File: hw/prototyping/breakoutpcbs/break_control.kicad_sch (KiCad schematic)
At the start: 21 parts, among them J11 Conn_01x07, J12 Conn_01x07, J13 Conn_01x06, J15 Conn_01x04, J16 Screw_Terminal_01x04, J17 Conn_01x05, J18 Screw_Terminal_01x04, Q10 BC337, Q11 BC847

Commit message: fixed wrong pinout on rf module and updated footprints
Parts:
- removed M2: ~, chinese_modules:RF_controller, symbol chinese_modules:RF_controller
- added M3: ~, chinese_modules:RF_controller, symbol chinese_modules:RF_controller
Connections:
- net +5V_1: now also M3.6 (V+)
- net GND4: now also M3.7 (GND)
- net at R40.2: now also M3.5 (D0)
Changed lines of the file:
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@@
-	)
-	(symbol
-		(lib_id "chinese_modules:RF_controller")
-		(at 67.31 48.26 0)
-		(unit 1)
-		(exclude_from_sim no)
-		(in_bom yes)
-		(on_board yes)
-		(dnp no)
-		(fields_autoplaced yes)
-		(property "Reference" "M2"
-			(at 67.31 34.29 0)
-			(effects
-				(font
-					(size 1.27 1.27)
-				)
-			)
-		)
-		(property "Value" "~"
-			(at 67.31 36.83 0)
-			(effects
-				(font
-					(size 1.27 1.27)
-				)
-			)
-		)
-		(property "Footprint" "chinese_modules:RF_controller"
-			(at 67.31 48.26 0)
-			(effects
-				(font
-					(size 1.27 1.27)
-				)
-				(hide yes)
-			)
-		)
-		(property "Datasheet" ""
-			(at 67.31 48.26 0)
-			(effects
-				(font
-					(size 1.27 1.27)
-				)
-				(hide yes)
-			)
-		)
-		(property "Description" ""
-			(at 67.31 48.26 0)
-			(effects
-				(font
-					(size 1.27 1.27)
-				)
-				(hide yes)
-			)
-		)
-		(pin "8"
-		)
-		(pin "2"
-		)
-		(pin "1"
-		)
-		(pin "5"
-		)
-		(pin "6"
-		)
-		(pin "7"
-		)
-		(pin "3"
-		)
-		(pin "4"
-		)
-		(instances
-			(project "breakoutpcbs"
-				(path "/164def8b-47e5-45df-ad5a-f5307e8b0f23/6473b973-a331-47c6-86ec-edf4d9af8870"
-					(reference "M2")
-					(unit 1)
-				)
-			)
-		)
 	)
 	(symbol
@@
 					(unit 1)
 				)
+			)
+		)
+	)
+	(symbol
+		(lib_name "RF_controller_1")
+		(lib_id "chinese_modules:RF_controller")
+		(at 67.31 48.26 0)
+		(unit 1)
+		(exclude_from_sim no)
+		(in_bom yes)
+		(on_board yes)
+		(dnp no)
+		(fields_autoplaced yes)
+		(property "Reference" "M3"
+			(at 67.31 34.29 0)
+			(effects
+				(font
+					(size 1.27 1.27)
+				)
+			)
+		)
+		(property "Value" "~"
+			(at 67.31 36.83 0)
+			(effects
+				(font
+					(size 1.27 1.27)
+				)
+			)
+		)
+		(property "Footprint" "chinese_modules:RF_controller"
+			(at 67.31 48.26 0)
+			(effects
+				(font
+					(size 1.27 1.27)
+				)
+				(hide yes)
+			)
+		)
+		(property "Datasheet" ""
+			(at 67.31 48.26 0)
+			(effects
+				(font
+					(size 1.27 1.27)
+				)
+				(hide yes)
+			)
+		)
+		(property "Description" ""
+			(at 67.31 48.26 0)
+			(effects
+				(font
+					(size 1.27 1.27)
+				)
+				(hide yes)
+			)
+		)
+		(pin "7"
+		)
+		(pin "4"
+		)
+		(pin "3"
+		)
+		(pin "5"
+		)
+		(pin "6"
+		)
+		(pin "2"
+		)
+		(pin "1"
+		)
+		(pin "8"
+		)
+		(instances
+			(project ""
+				(path "/164def8b-47e5-45df-ad5a-f5307e8b0f23/6473b973-a331-47c6-86ec-edf4d9af8870"
+					(reference "M3")
+					(unit 1)
+				)

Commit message: updated schematics
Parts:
- R40: value 4k7 -> 2k7
- R41: value 10k -> 4k7
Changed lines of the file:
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@@
 			)
 		)
-		(property "Value" "10k"
+		(property "Value" "4k7"
 			(at 98.552 48.26 0)
 			(effects
@@
 			)
 		)
-		(property "Value" "4k7"
+		(property "Value" "2k7"
 			(at 87.63 46.736 90)
 			(effects

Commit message: todos update
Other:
- note added: "TODO: - anode RGB led resistor 1k2 - remove resistors at the cathodes on the RGB LED - 5V DC/DC convertor (stepdown) - connect ledbar to the 5v and make it use the 3v3 while the charging"
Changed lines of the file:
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@@
+		)
+	)
+	(text "TODO: \n- anode RGB led resistor 1k2\n- remove resistors at the cathodes on the RGB LED\n- 5V DC/DC convertor (stepdown)\n- connect ledbar to the 5v and make it use the 3v3 while the charging"
+		(exclude_from_sim no)
+		(at 237.49 56.134 0)
+		(effects
+			(font
+				(size 1.27 1.27)
+			)
 		)
 	)

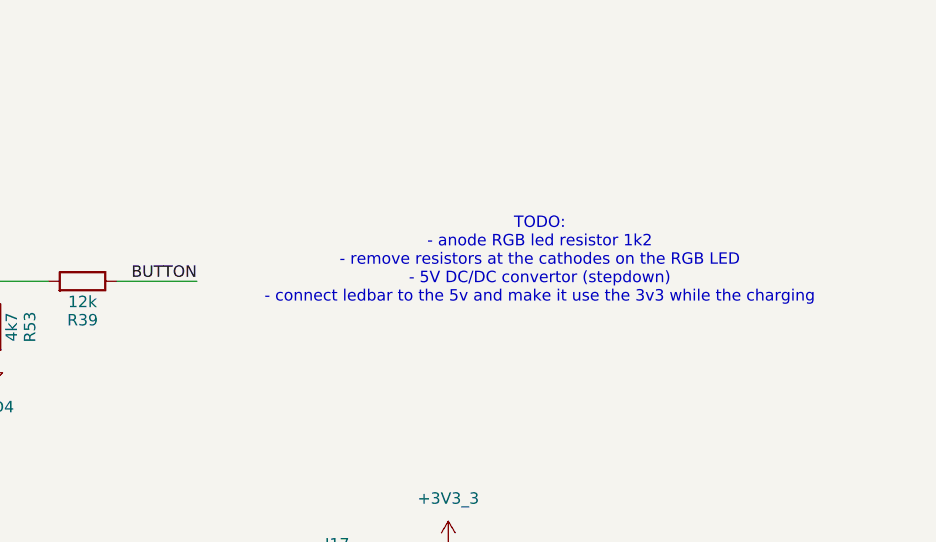
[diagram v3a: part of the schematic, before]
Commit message: added new todos
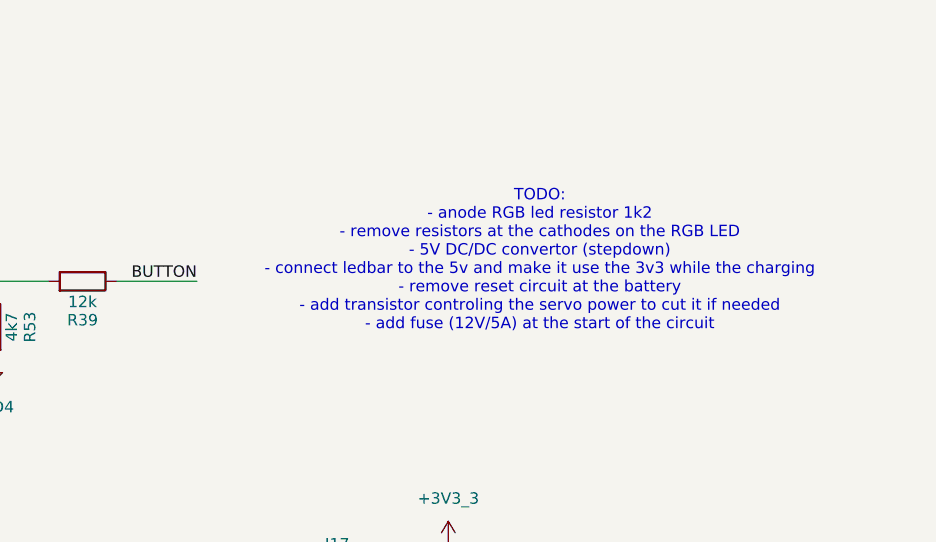
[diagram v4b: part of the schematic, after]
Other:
- note added: "TODO: - anode RGB led resistor 1k2 - remove resistors at the cathodes on the RGB LED - 5V DC/DC convertor (stepdown) - connect ledbar to the 5v and make it use the 3v3 while the charging - remove reset circuit at the battery - add transistor controling the servo power to cut it if needed - add fuse (12V/5A) at the start of the circuit"
- note removed: "TODO: - anode RGB led resistor 1k2 - remove resistors at the cathodes on the RGB LED - 5V DC/DC convertor (stepdown) - connect ledbar to the 5v and make it use the 3v3 while the charging"
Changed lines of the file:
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@@
 		)
 	)
-	(text "TODO: \n- anode RGB led resistor 1k2\n- remove resistors at the cathodes on the RGB LED\n- 5V DC/DC convertor (stepdown)\n- connect ledbar to the 5v and make it use the 3v3 while the charging"
+	(text "TODO: \n- anode RGB led resistor 1k2\n- remove resistors at the cathodes on the RGB LED\n- 5V DC/DC convertor (stepdown)\n- connect ledbar to the 5v and make it use the 3v3 while the charging\n- remove reset circuit at the battery\n- add transistor controling the servo power to cut it if needed\n- add fuse (12V/5A) at the start of the circuit"
 		(exclude_from_sim no)
 		(at 237.49 56.134 0)

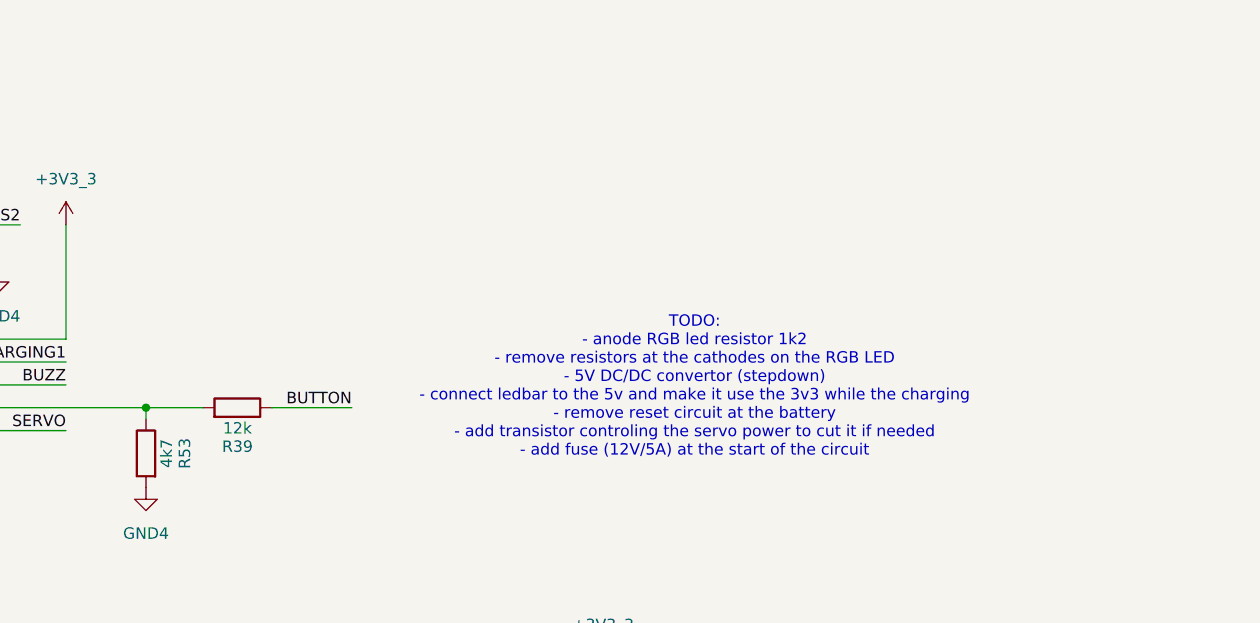
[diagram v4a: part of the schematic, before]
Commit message: updated kicad version and updated todo list with different found issues
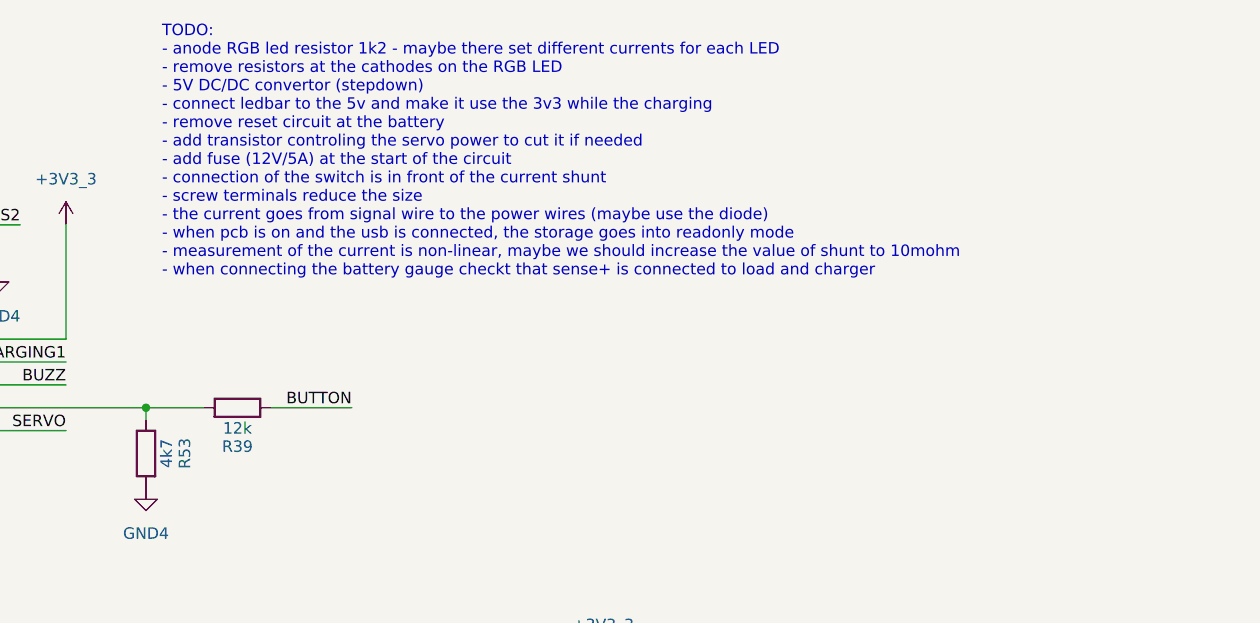
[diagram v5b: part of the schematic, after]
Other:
- note added: "TODO: - anode RGB led resistor 1k2 - maybe there set different currents for each LED - remove resistors at the cathodes on the RGB LED - 5V DC/DC convertor (stepdown) - connect ledbar to the 5v and make it use the 3v3 while the charging - remove reset circuit at the battery - add transistor controling the servo power to cut it if needed - add fuse (12V/5A) at the start of the circuit - connection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"
- note removed: "TODO: - anode RGB led resistor 1k2 - remove resistors at the cathodes on the RGB LED - 5V DC/DC convertor (stepdown) - connect ledbar to the 5v and make it use the 3v3 while the charging - remove reset circuit at the battery - add transistor controling the servo power to cut it if needed - add fuse (12V/5A) at the start of the circuit"
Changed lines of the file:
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@@
 (kicad_sch
-	(version 20241209)
+	(version 20250114)
 	(generator "eeschema")
 	(generator_version "9.0")
@@
 		)
 	)
-	(text "TODO: \n- anode RGB led resistor 1k2\n- remove resistors at the cathodes on the RGB LED\n- 5V DC/DC convertor (stepdown)\n- connect ledbar to the 5v and make it use the 3v3 while the charging\n- remove reset circuit at the battery\n- add transistor controling the servo power to cut it if needed\n- add fuse (12V/5A) at the start of the circuit"
+	(text "TODO: \n- anode RGB led resistor 1k2 - maybe there set different currents for each LED\n- remove resistors at the cathodes on the RGB LED\n- 5V DC/DC convertor (stepdown)\n- connect ledbar to the 5v and make it use the 3v3 while the charging\n- remove reset circuit at the battery\n- add transistor controling the servo power to cut it if needed\n- add fuse (12V/5A) at the start of the circuit\n- connection of the switch is in front of the current shunt\n- screw terminals reduce the size\n- the current goes from signal wire to the power wires (maybe use the diode)\n- when pcb is on and the usb is connected, the storage goes into readonly mode\n- measurement of the current is non-linear, maybe we should increase the value of shunt to 10mohm\n- when connecting the battery gauge checkt that sense+ is connected to load and charger"
 		(exclude_from_sim no)
-		(at 237.49 56.134 0)
+		(at 178.308 29.972 0)
 		(effects
 			(font
 				(size 1.27 1.27)
 			)
+			(justify left)
 		)
 	)
